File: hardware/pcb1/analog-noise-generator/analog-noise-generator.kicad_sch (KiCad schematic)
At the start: 67 parts, among them J1 USB_C_Receptacle_USB2.0, J2 Conn_01x03, J3 PJ-211A, J4 PJ-211A, J5 Conn_01x04_Pin, J6 Conn_01x04_Pin, J7 Conn_01x02_Pin, U1 STM32F072CBTx, U2 USBLC6-2SC6, U3 LR8321A-T33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

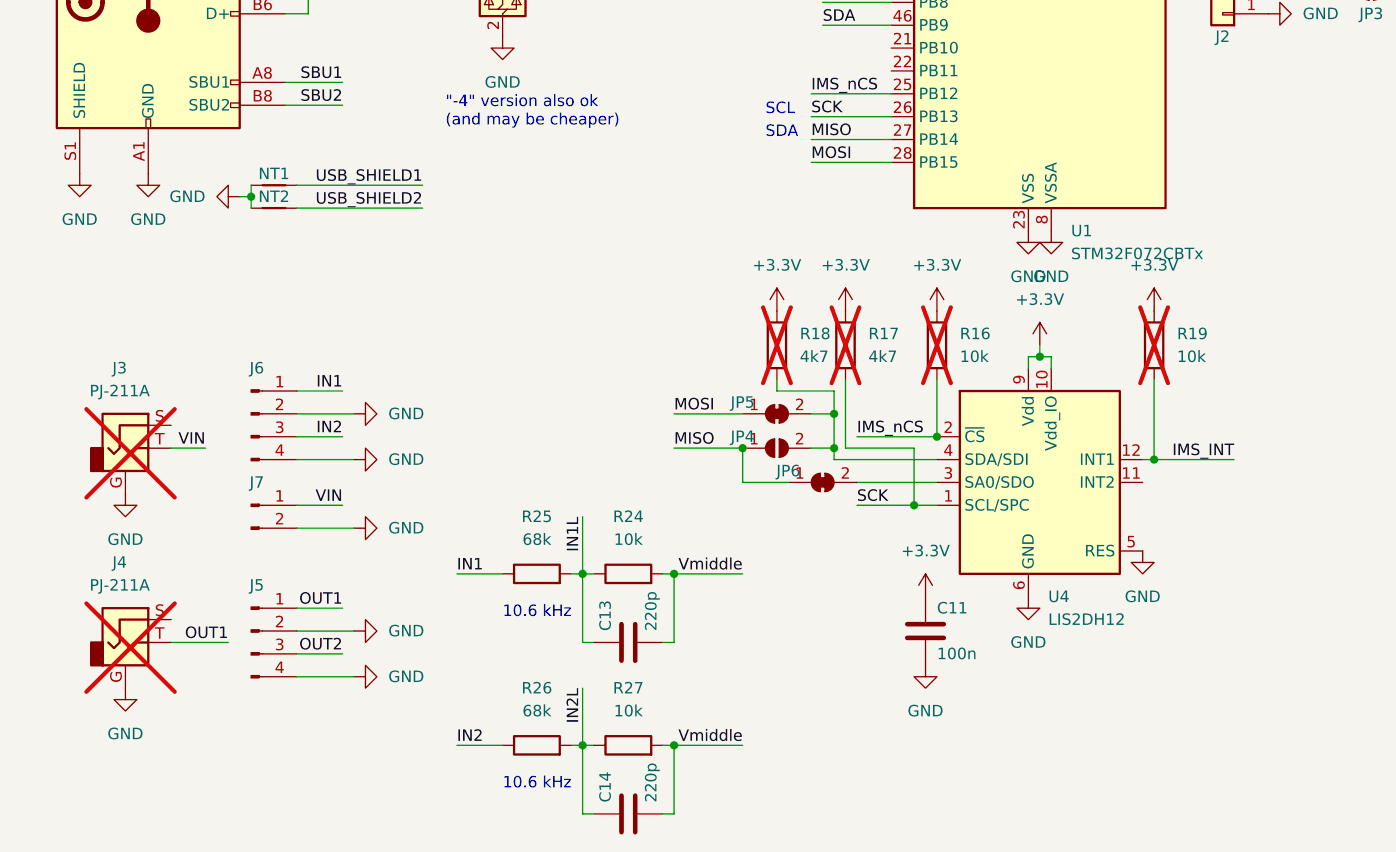
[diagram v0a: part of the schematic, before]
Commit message: fix some violations
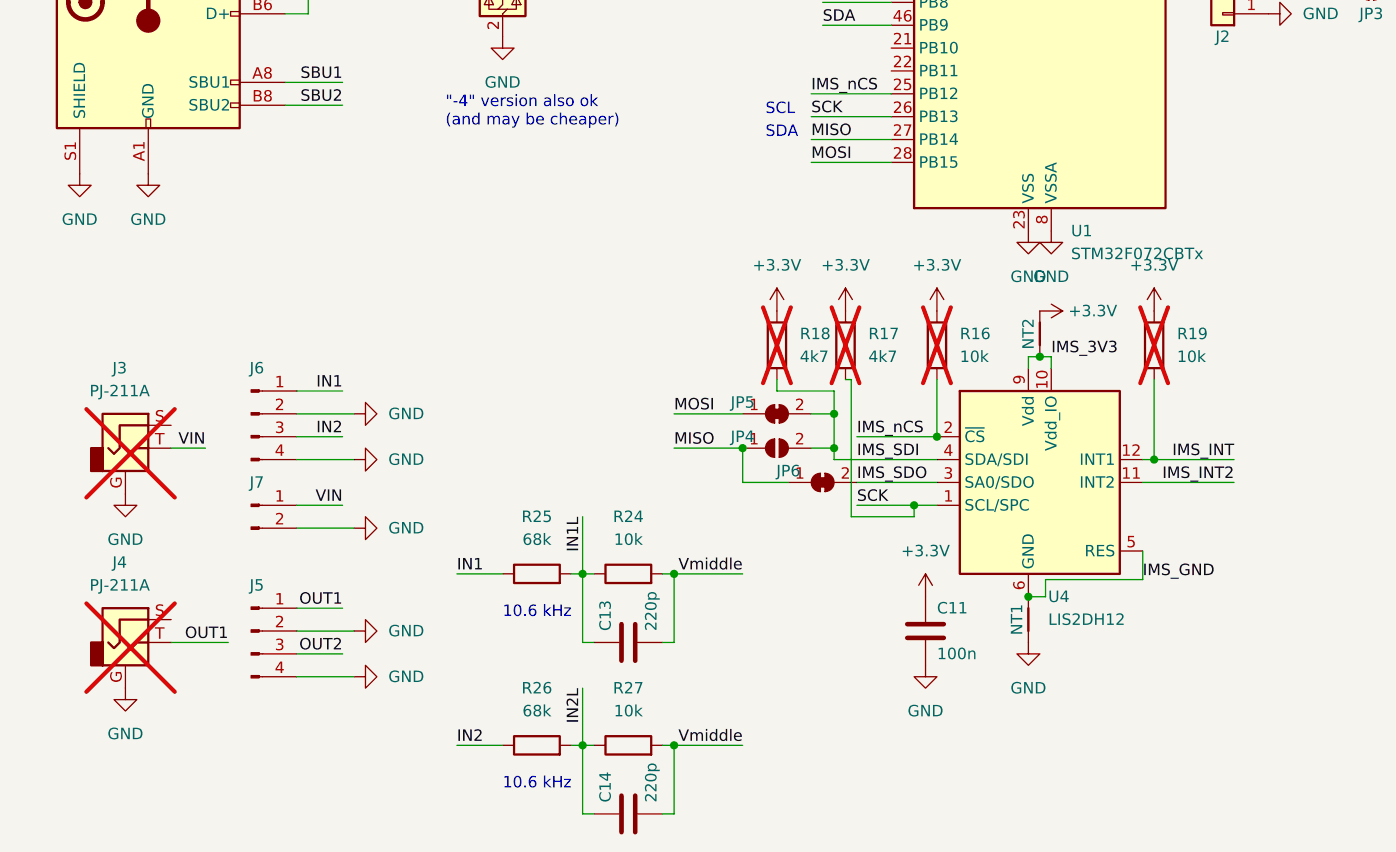
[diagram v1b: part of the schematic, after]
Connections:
- net USB_SHIELD2 is gone; now on net +3.3V: NT2.1
- net +3.3V: no longer U4.10 (Vdd_IO), U4.9 (Vdd)
- net GND: no longer NT2.2, U4.5 (RES), U4.6 (GND), U4.7 (GND), U4.8 (GND)
- net IMS_INT2: now reaches U4.11 (INT2)
- net IMS_SDO: now reaches JP6.2 (B), U4.3 (SA0/SDO)
- net IMS_SDI: now reaches JP4.2 (B), JP5.2 (B), R18.1, U4.4 (SDA/SDI)
- net USB_SHIELD1 renamed IMS_GND
- net IMS_GND: now also U4.5 (RES), U4.6 (GND), U4.7 (GND), U4.8 (GND)
- new net IMS_3V3: NT2.2, U4.10 (Vdd_IO), U4.9 (Vdd)
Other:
- moved on the sheet: NT1, NT2

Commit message: continue
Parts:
- added TP5: -V, analog-noise-generator:TestPoint_THTPad_small, symbol Connector:TestPoint_Probe
- TP4: value VIN -> +V
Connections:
- net +8V: now also TP4.1
- net -8V: now also TP5.1
- net VIN: no longer TP4.1
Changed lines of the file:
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@@
     (stroke (width 0) (type default))
   )
+  (wire (pts (xy 55.88 54.61) (xy 57.15 54.61))
+    (stroke (width 0) (type default))
+  )
   (wire (pts (xy 58.42 111.76) (xy 64.77 111.76))
     (stroke (width 0) (type default))
@@
     )
   )
+  (symbol (lib_id "Connector:TestPoint_Probe") (at 57.15 54.61 0) (mirror x) (unit 1)
+    (in_bom no) (on_board yes) (dnp no)
+    (property "Reference" "TP5" (at 60.96 58.42 0)
+      (effects (font (size 1.27 1.27)) (justify left))
+    )
+    (property "Value" "-V" (at 60.96 55.88 0)
+      (effects (font (size 1.27 1.27)) (justify left))
+    )
+    (property "Footprint" "analog-noise-generator:TestPoint_THTPad_small" (at 62.23 54.61 0)
+      (effects (font (size 1.27 1.27)) hide)
+    )
+    (property "Datasheet" "~" (at 62.23 54.61 0)
+      (effects (font (size 1.27 1.27)) hide)
+    )
+    (pin "1")
+    (instances
+      (project "analog-noise-generator"
+        (path "/e71fa5ad-0f80-45ec-aa84-70ffc489027a"
+          (reference "TP5") (unit 1)
+        )
+      )
+    )
+  )
   (symbol (lib_id "power:GND") (at 138.43 27.94 0) (unit 1)
     (in_bom yes) (on_board yes) (dnp no) (fields_autoplaced)
@@
     )
   )
+  (symbol (lib_id "Connector:TestPoint_Probe") (at 55.88 22.86 0) (unit 1)
+    (in_bom no) (on_board yes) (dnp no)
+    (property "Reference" "TP4" (at 59.69 19.05 0)
+      (effects (font (size 1.27 1.27)) (justify left))
+    )
+    (property "Value" "+V" (at 59.69 21.59 0)
+      (effects (font (size 1.27 1.27)) (justify left))
+    )
+    (property "Footprint" "analog-noise-generator:TestPoint_THTPad_small" (at 60.96 22.86 0)
+      (effects (font (size 1.27 1.27)) hide)
+    )
+    (property "Datasheet" "~" (at 60.96 22.86 0)
+      (effects (font (size 1.27 1.27)) hide)
+    )
+    (pin "1")
+    (instances
+      (project "analog-noise-generator"
+        (path "/e71fa5ad-0f80-45ec-aa84-70ffc489027a"
+          (reference "TP4") (unit 1)
+        )
+      )
+    )
+  )
   (symbol (lib_id "power:+BATT") (at 123.19 20.32 0) (unit 1)
     (in_bom yes) (on_board yes) (dnp no) (fields_autoplaced)
@@
         )
       )
-    )
-  )
-  (symbol (lib_id "Connector:TestPoint_Probe") (at 38.1 22.86 0) (mirror y) (unit 1)
-    (in_bom no) (on_board yes) (dnp no)
-    (property "Reference" "TP4" (at 34.29 19.05 0)
-      (effects (font (size 1.27 1.27)) (justify left))
-    )
-    (property "Value" "VIN" (at 34.29 21.59 0)
-      (effects (font (size 1.27 1.27)) (justify left))
-    )
-    (property "Footprint" "analog-noise-generator:TestPoint_THTPad_small" (at 33.02 22.86 0)
-      (effects (font (size 1.27 1.27)) hide)
-    )
-    (property "Datasheet" "~" (at 33.02 22.86 0)
-      (effects (font (size 1.27 1.27)) hide)
-    )
-    (pin "1")
-    (instances
-      (project "analog-noise-generator"
-        (path "/e71fa5ad-0f80-45ec-aa84-70ffc489027a"
-          (reference "TP4") (unit 1)
-        )
-      )

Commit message: continue
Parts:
- removed J2: Conn_01x03, Connector_PinHeader_2.54mm:PinHeader_1x03_P2.54mm_Vertical, symbol Connector_Generic:Conn_01x03
- removed R13: 100R, Resistor_SMD:R_0402_1005Metric, symbol Device:R
- added C15, C18, C19: 220p, Capacitor_SMD:C_0402_1005Metric, symbol Device:C
- added C16, C17: 100n, 50V, Capacitor_SMD:C_0402_1005Metric, symbol Device:C
- added D3: ~, Diode_SMD:D_SOD-323, symbol Device:D_Schottky
- added J2: Conn_01x04_Pin, Connector_PinHeader_2.54mm:PinHeader_1x04_P2.54mm_Vertical, symbol Connector:Conn_01x04_Pin
- added JP10, JP7, JP9: SolderJumper_2_Bridged, Jumper:SolderJumper-2_P1.3mm_Bridged_RoundedPad1.0x1.5mm, symbol Jumper:SolderJumper_2_Bridged
- added JP11, JP8: SolderJumper_2_Open, Jumper:SolderJumper-2_P1.3mm_Open_RoundedPad1.0x1.5mm, symbol Jumper:SolderJumper_2_Open
- added R28, R29: 4k7, Resistor_SMD:R_0805_2012Metric_Pad1.20x1.40mm_HandSolder, symbol Device:R
- C12: value 100n -> 100n, 50V; LCSC C1525 -> (none)
- C9: LCSC C1525 -> (none)
- R14: value 10k -> 68k; LCSC C25744 -> (none)
- R15: value 5.1k -> 10k; LCSC C25905 -> C25744
- R16, R17, R18, R19: footprint Resistor_SMD:R_0402_1005Metric -> Resistor_SMD:R_0805_2012Metric_Pad1.20x1.40mm_HandSolder
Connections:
- net -8V is gone; now on net -9VA: C10.2, R11.1, TP5.1
- net +3.3V: now also JP8.2 (B), R28.2, R29.2; no longer C12.1, U5.4 (V+)
- net +8V: now also D1.1 (K), D3.1 (K); no longer R5.2
- net BOOT0: now also J2.1 (Pin_1), JP7.2 (B); no longer R6.2, R7.2, U1.43 (PB7)
- net GND: now also R15.1, C15.2, C16.2, C17.1, C18.2, J2.2 (Pin_2), JP11.1 (A); no longer C12.2, R15.2, U5.11 (V-)
- net SCL: now also R28.1
- net SDA: now also R29.1
- net SWCLK: now also J2.3 (Pin_3)
- net SWDIO: now also J2.4 (Pin_4)
- net V+_sense: now also C15.1
- net V-_sense: now also C19.1
- net VBUS: now also D3.2 (A)
- net VIN: now also R5.2; no longer J7.1 (Pin_1)
- net VIN_sense: now also R15.2, C18.1; no longer R15.1
- net -9VA: now reaches D2.2 (A)
- net -9VA: now also C19.2, JP10.1 (A)
- net at R5.1: now also J7.1 (Pin_1); no longer D1.1 (K)
- new net: C12.1, C16.1, JP8.1 (A), JP9.1 (A), U5.4 (V+)
- new net: C12.2, C17.2, JP10.2 (B), JP11.2 (B), U5.11 (V-)
- new net +9VA: JP9.2 (B)
- new net VUSB_DET: JP7.1 (A), R6.2, R7.2, U1.43 (PB7)
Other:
- note added: "comparator: 4/4: 9.8 V 3/4: 7.3 V 2/4: 4.9 V 1/4: 2.4 V"
- moved on the sheet: C12, R5, U5E

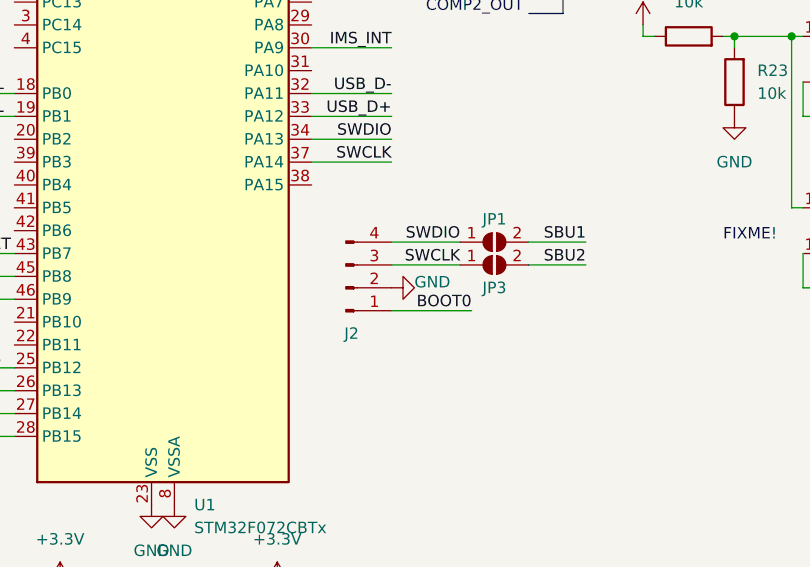
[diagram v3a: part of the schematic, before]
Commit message: shorten the board a bit
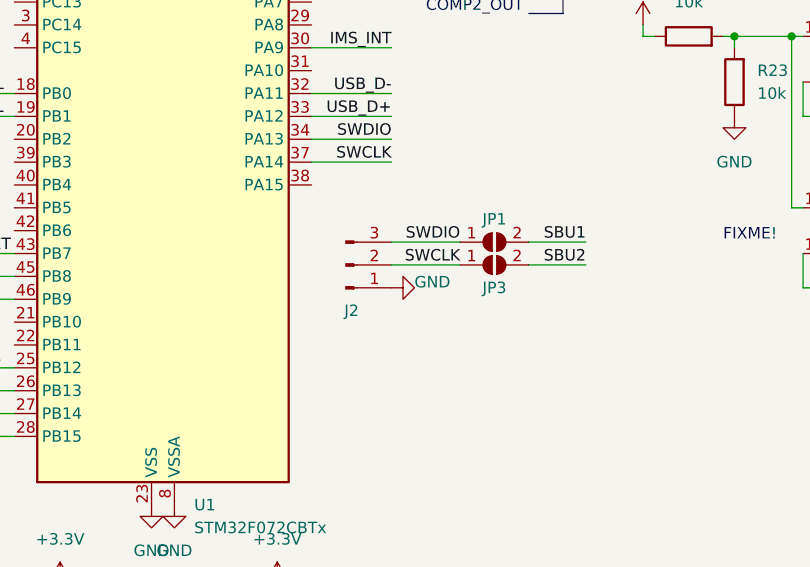
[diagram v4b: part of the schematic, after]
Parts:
- J2: value Conn_01x04_Pin -> Conn_01x03_Pin; footprint Connector_PinHeader_2.54mm:PinHeader_1x04_P2.54mm_Vertical -> Connector_PinHeader_2.54mm:PinHeader_1x03_P2.54mm_Vertical; symbol Connector:Conn_01x04_Pin -> Connector:Conn_01x03_Pin
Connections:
- net BOOT0: no longer J2.1 (Pin_1)
- net GND: now also J2.1 (Pin_1); no longer J2.2 (Pin_2)
- net SWCLK: now also J2.2 (Pin_2); no longer J2.3 (Pin_3)
- net SWDIO: now also J2.3 (Pin_3); no longer J2.4 (Pin_4)
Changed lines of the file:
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@@
-    (stroke (width 0) (type default))
-  )
-  (wire (pts (xy 167.64 104.14) (xy 176.53 104.14))
     (stroke (width 0) (type default))
   )
@@
   )
   (label "NRST" (at 88.9 49.53 180) (fields_autoplaced)
-    (effects (font (size 1.27 1.27)) (justify right bottom))
-  )
-  (label "BOOT0" (at 176.53 104.14 180) (fields_autoplaced)
     (effects (font (size 1.27 1.27)) (justify right bottom))
   )
@@
     )
   )
-  (symbol (lib_id "Connector:Conn_01x04_Pin") (at 162.56 101.6 0) (mirror x) (unit 1)
+  (symbol (lib_id "Connector:Conn_01x03_Pin") (at 162.56 99.06 0) (mirror x) (unit 1)
     (in_bom yes) (on_board yes) (dnp no)
-    (property "Reference" "J2" (at 163.195 106.68 0)
-      (effects (font (size 1.27 1.27)))
-    )
-    (property "Value" "Conn_01x04_Pin" (at 163.195 106.68 0)
-      (effects (font (size 1.27 1.27)) hide)
-    )
-    (property "Footprint" "Connector_PinHeader_2.54mm:PinHeader_1x04_P2.54mm_Vertical" (at 162.56 101.6 0)
-      (effects (font (size 1.27 1.27)) hide)
-    )
-    (property "Datasheet" "~" (at 162.56 101.6 0)
+    (property "Reference" "J2" (at 163.195 104.14 0)
+      (effects (font (size 1.27 1.27)))
+    )
+    (property "Value" "Conn_01x03_Pin" (at 162.56 93.98 0)
+      (effects (font (size 1.27 1.27)) hide)
+    )
+    (property "Footprint" "Connector_PinHeader_2.54mm:PinHeader_1x03_P2.54mm_Vertical" (at 162.56 99.06 0)
+      (effects (font (size 1.27 1.27)) hide)
+    )
+    (property "Datasheet" "~" (at 162.56 99.06 0)
       (effects (font (size 1.27 1.27)) hide)
     )
@@
     (pin "3")
     (pin "1")
-    (pin "4")
-    (instances
-      (project "analog-noise-generator"
+    (instances
+      (project "analog-noise-generator"

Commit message: continue
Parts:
- added J9: Conn_02x04_Odd_Even, Connector_PinSocket_2.54mm:PinSocket_2x04_P2.54mm_Vertical_SMD, symbol Connector_Generic:Conn_02x04_Odd_Even
- added TP6: TOUCH1, analog-noise-generator:TestPoint_THTPad_small, symbol Connector:TestPoint_Probe
- added TP7: TOUCH2, analog-noise-generator:TestPoint_THTPad_small, symbol Connector:TestPoint_Probe
- D1, D2, D3: LCSC C181207 -> C191023
- R14, R25, R26: footprint Resistor_SMD:R_0402_1005Metric -> Resistor_SMD:R_0603_1608Metric; LCSC (none) -> C23231
- R17, R18, R28, R29: LCSC (none) -> C25900
- R5: LCSC (none) -> C25076
- U1: LCSC (none) -> C81720
- U5: LCSC (none) -> C71035
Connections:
- net +9VA is gone; now on net +8V: JP9.2 (B)
- net +3.3V: now also J9.8 (Pin_8)
- net GND: now also J6.1 (Pin_1), J6.3 (Pin_3), J9.7 (Pin_7); no longer J6.2 (Pin_2), J6.4 (Pin_4)
- net IN1: now also J6.4 (Pin_4); no longer J6.1 (Pin_1)
- net IN2: now also J7.1 (Pin_1); no longer J6.3 (Pin_3)
- net MOSI: now also J9.6 (Pin_6)
- net SCK: now also J9.5 (Pin_5)
- net TOUCH1: now reaches U1.16 (PA6)
- net TOUCH1: now also TP6.1
- net TOUCH2: now reaches U1.17 (PA7)
- net TOUCH2: now also TP7.1
- net PUMP_VNEG: now reaches U1.2 (PC13)
- net EPD_BUSY: now reaches U1.3 (PC14)
- net EPD_BUSY: now also J9.1 (Pin_1)
- net EPD_DC: now reaches U1.4 (PC15)
- net EPD_DC: now also J9.3 (Pin_3)
- net EPD_CS: now reaches U1.5 (PF0)
- net EPD_CS: now also J9.4 (Pin_4)
- net EPD_RES: now reaches U1.6 (PF1)
- net EPD_RES: now also J9.2 (Pin_2)
- net VIN': now reaches R5.1
- net VIN': now also J6.2 (Pin_2); no longer J7.1 (Pin_1)
- net -9VA renamed -8V
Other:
- note added: "EPD_SCL"
- note added: "EPD_SDA"
- note added: "maybe replace by HT75331 (basic part)"
- moved on the sheet: C9, R5, R8
